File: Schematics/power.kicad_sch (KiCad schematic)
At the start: 12 parts, among them Q6 Q_PMOS_GSD, U3 PowerIn, U4 LDL1117-3.3

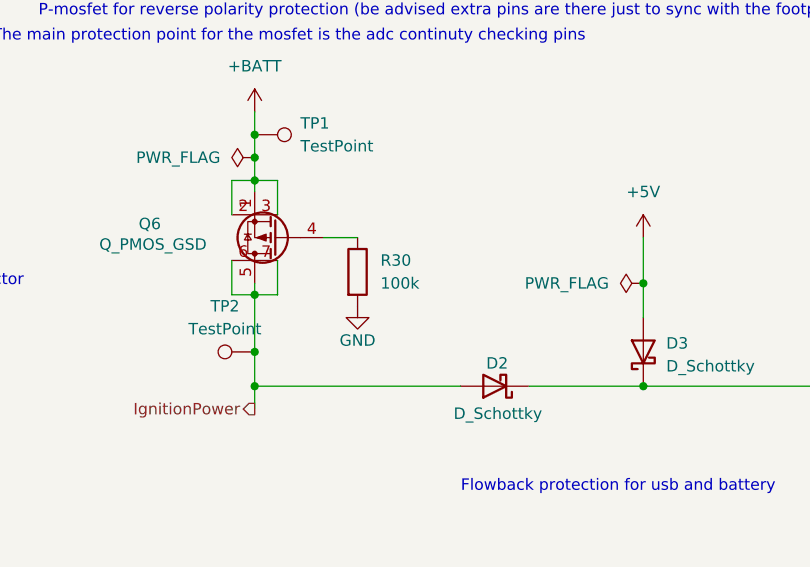
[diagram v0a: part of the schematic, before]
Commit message: ran dmf check fixed some things
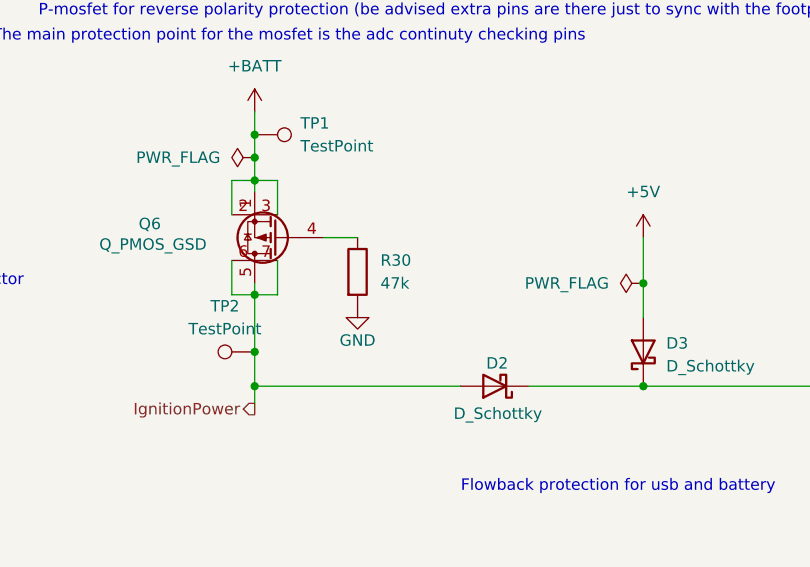
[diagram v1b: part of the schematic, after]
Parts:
- R30: value 100k -> 47k; LCSC C96346 -> C2933415
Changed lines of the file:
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@@
 			)
 		)
-		(property "Value" "100k"
+		(property "Value" "47k"
 			(at 101.6 87.6299 0)
 			(effects
@@
 			)
 		)
-		(property "LCSC" "C96346"
+		(property "LCSC" "C2933415"
 			(at 99.06 86.36 0)
 			(effects
